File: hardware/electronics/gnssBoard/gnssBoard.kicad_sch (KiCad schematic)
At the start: 22 parts, among them J1 Standoff, J2 M.2_E_Key_PCB_Edge, U1 AP7361E

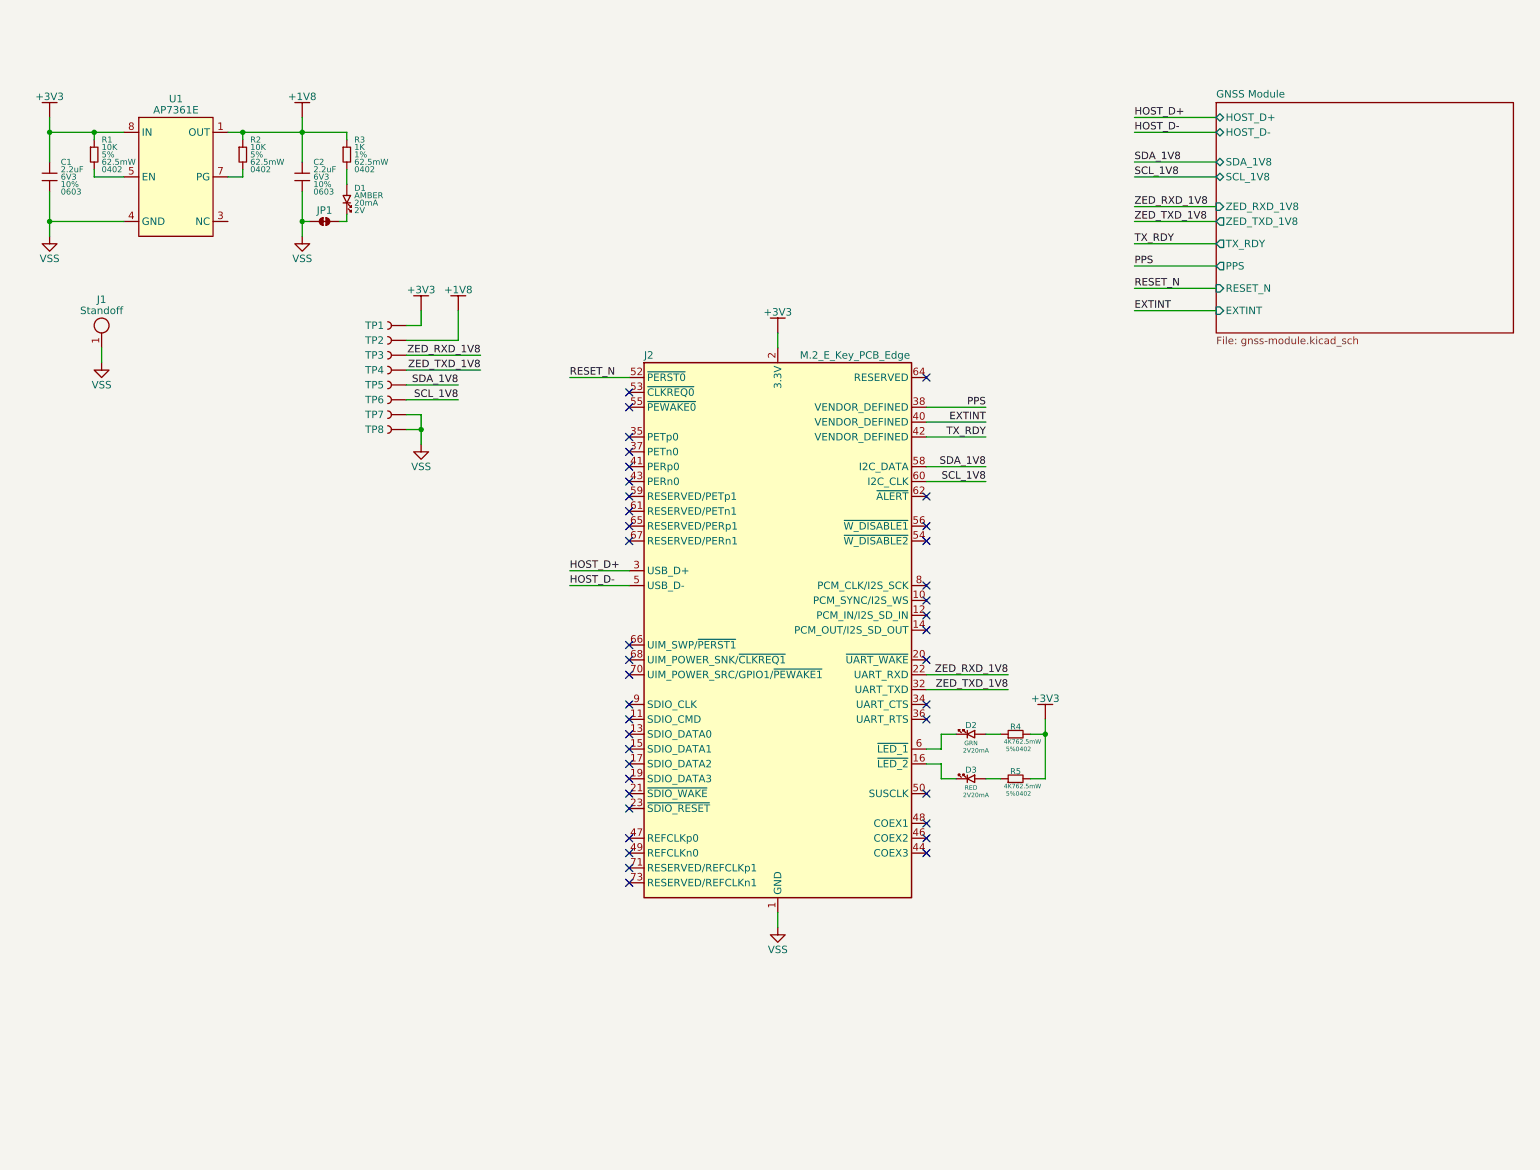
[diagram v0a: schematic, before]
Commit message: cleaned up schematic
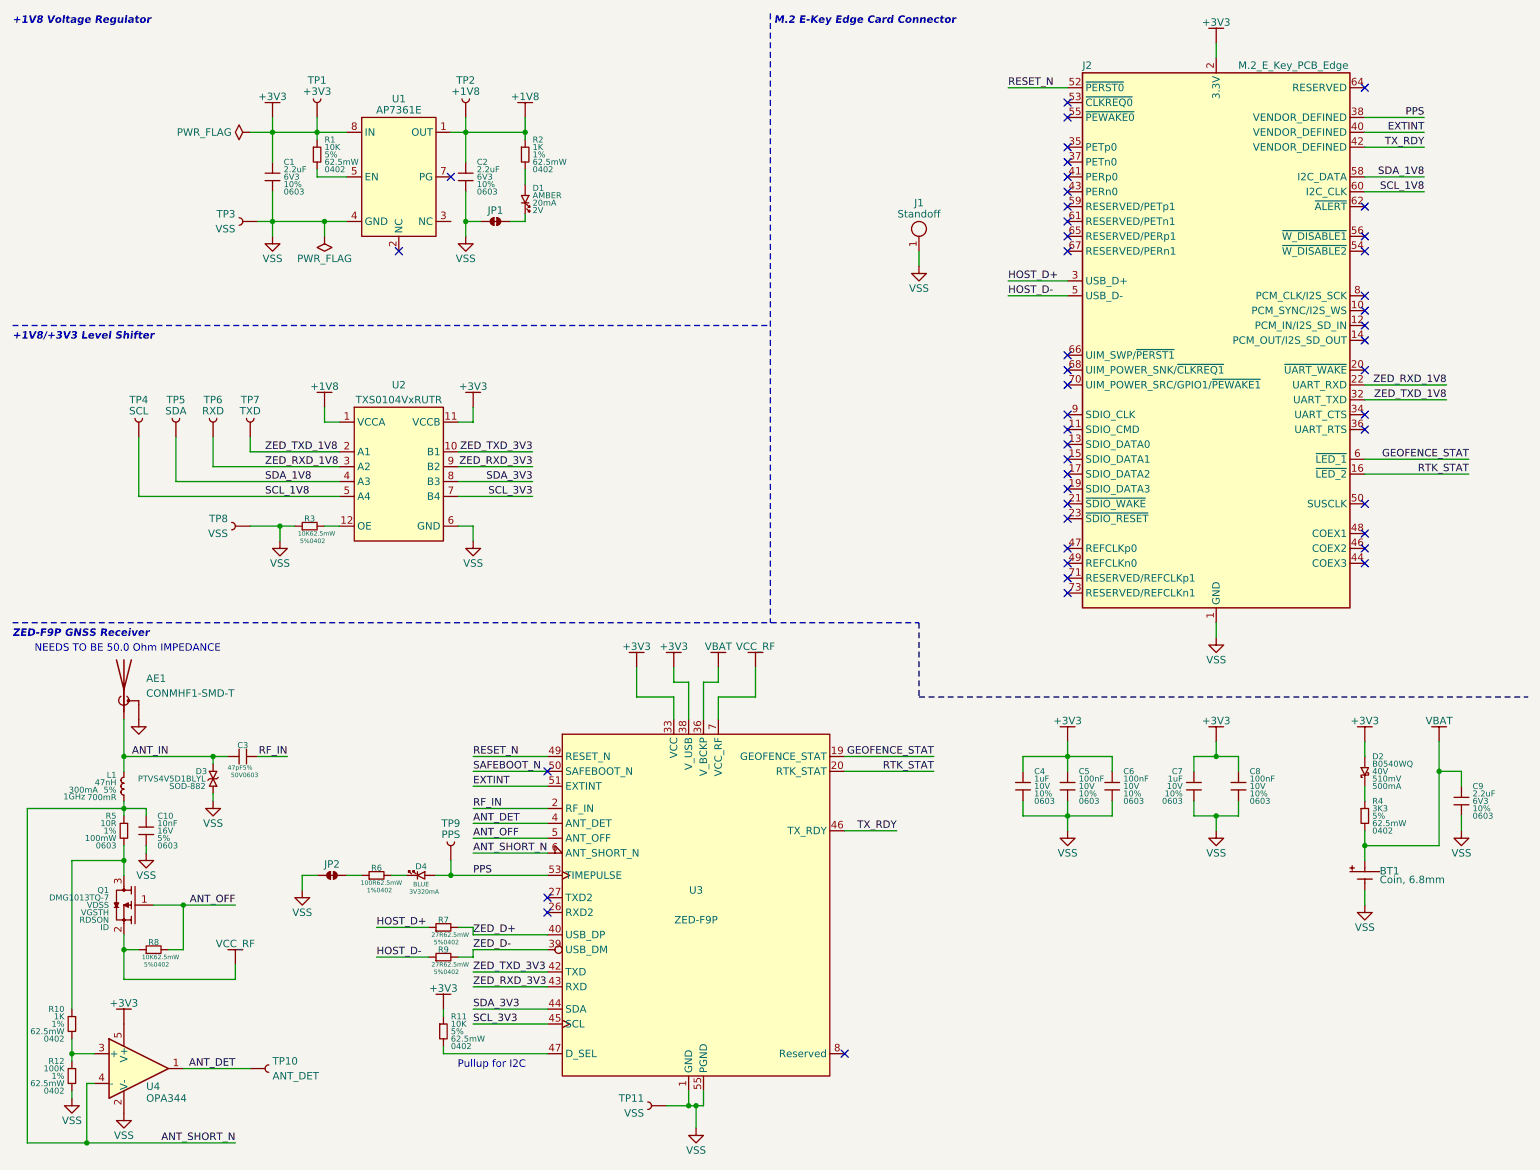
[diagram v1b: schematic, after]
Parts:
- removed D2: LTST-C190KGKT, lib_fp:LTST-0603, symbol lib_sch:LED_horizontal_1
- removed D3: LTST-C190KRKT, lib_fp:LTST-0603, symbol lib_sch:LED_horizontal_1
- removed R2: 10K, lib_fp:CRCW0402, symbol lib_sch:R
- removed R4, R5: 4K7, lib_fp:CRCW0402, symbol lib_sch:R_horizontal
- removed TP3, TP8: ~, lib_fp:TP_1mm, symbol lib_sch:Testpoint
- added AE1: CONMHF1-SMD-T, lib_fp:CONMHF1, symbol lib_sch:Antenna_Shield
- added BT1: ~, lib_fp:MS621FE-FL11E, symbol lib_sch:Battery
- added C10: 10nF, lib_fp:MLCC0603, symbol lib_sch:C
- added C3: 47pF, lib_fp:MLCC0603, symbol lib_sch:C_horizontal
- added C4, C7: 1uF, lib_fp:MLCC0603, symbol lib_sch:C
- added C5, C6, C8: 100nF, lib_fp:MLCC0603, symbol lib_sch:C
- added C9: 2.2uF, lib_fp:MLCC0603, symbol lib_sch:C
- added D2: B0540WQ, lib_fp:SOD123, symbol lib_sch:D_Schottky
- added D3: PTVS4V5D1BLYL, lib_fp:SOD882, symbol lib_sch:D_TVS
- added D4: LTST-C190KRKT, lib_fp:LTST-0603, symbol lib_sch:LED_horizontal_1
- added JP2: ~, lib_fp:SolderJumper-2_P1.3mm_Bridged_Pad1.0x1.5mm, symbol lib_sch:Jumper_2_Bridged
- added L1: 47nH, lib_fp:L_0402, symbol lib_sch:L
- added Q1: DMG1013TQ-7, lib_fp:SOT23-3P50_160X160X75L22X22N, symbol lib_sch:PMOS_DGS
- added R10: 1K, lib_fp:CRCW0402, symbol lib_sch:R
- added R11: 10K, lib_fp:CRCW0402, symbol lib_sch:R
- added R12: 100K, lib_fp:CRCW0402, symbol lib_sch:R
- added R3, R8: 10K, lib_fp:CRCW0402, symbol lib_sch:R_horizontal
- added R4: 3K3, lib_fp:CRCW0402, symbol lib_sch:R
- added R5: 10R, lib_fp:CRCW0603, symbol lib_sch:R
- added R6: 100R, lib_fp:CRCW0402, symbol lib_sch:R_horizontal
- added R7, R9: 27R, lib_fp:CRCW0402, symbol lib_sch:R_horizontal
- added TP10: ANT_DET, lib_fp:TP_1mm, symbol lib_sch:Testpoint_horizontal
- added TP11, TP3, TP8: VSS, lib_fp:TP_1mm, symbol lib_sch:Testpoint_horizontal
- added TP9: PPS, lib_fp:TP_1mm, symbol lib_sch:Testpoint
- added U2: TXS0104VxRUTR, lib_fp:RUT0012A, symbol lib_sch:TXS0104VxRUTR
- added U3: ZED-F9P, lib_fp:ZED-F9P-04B_UBL, symbol lib_sch:ZED-F9P-04B
- added U4: OPA344, lib_fp:SOT23-5P95_280X300X110L40X38N, symbol lib_sch:TS391
- J2: DKPN N/A -> (none); MPN N/A -> (none); Manufacturer N/A -> (none); now in the parts list
- JP1: footprint lib_fp:Jumper_2_Bridged -> lib_fp:SolderJumper-2_P1.3mm_Bridged_Pad1.0x1.5mm
- TP1: value ~ -> +3V3
- TP2: value ~ -> +1V8
- TP4: value ~ -> SCL
- TP5: value ~ -> SDA
- TP6: value ~ -> RXD
- TP7: value ~ -> TXD
- renumbered R3 to R2
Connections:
- net +1V8: now also U2.1 (VCCA)
- net +3V3: now also C4.1, C5.1, C6.1, C7.1, C8.1, D2.1, R11.1, U2.11 (VCCB), U3.33 (VCC), U3.34 (VCC), U3.38 (V_USB), U4.5 (V+)
- net EXTINT: now also U3.51 (EXTINT)
- net HOST_D+: now also R7.1
- net HOST_D-: now also R9.1
- net PPS: now also D4.1, TP9.1, U3.53 (TIMEPULSE)
- net RESET_N: now also U3.49 (RESET_N)
- net SCL_1V8: now also TP4.1, U2.5 (A4); no longer TP6.1
- net SDA_1V8: now also U2.4 (A3)
- net TX_RDY: now also U3.46 (TX_RDY)
- net VSS: now also AE1.2 (Shield), BT1.2, C10.2, C4.2, C5.2, C6.2, C7.2, C8.2, C9.2, D3.1, JP2.2, R12.2, R3.1, TP11.1, TP3.1, TP8.1, U2.6 (GND), U3.1 (GND), U3.100 (PGND), U3.101 (PGND), U3.102 (PGND), U3.12 (GND), U3.14 (GND), U3.3 (GND), U3.32 (GND), U3.37 (GND), U3.41 (GND), U3.48 (GND), U3.55 (PGND), U3.56 (PGND), U3.57 (PGND), U3.58 (PGND), U3.59 (PGND), U3.60 (PGND), U3.61 (PGND), U3.62 (PGND), U3.63 (PGND), U3.64 (PGND), U3.65 (PGND), U3.66 (PGND), U3.67 (PGND), U3.68 (PGND), U3.69 (PGND), U3.70 (PGND), U3.71 (PGND), U3.72 (PGND), U3.73 (PGND), U3.74 (PGND), U3.75 (PGND), U3.76 (PGND), U3.77 (PGND), U3.78 (PGND), U3.79 (PGND), U3.80 (PGND), U3.81 (PGND), U3.82 (PGND), U3.83 (PGND), U3.84 (PGND), U3.85 (PGND), U3.86 (PGND), U3.87 (PGND), U3.88 (PGND), U3.89 (PGND), U3.90 (PGND), U3.91 (PGND), U3.92 (PGND), U3.93 (PGND), U3.94 (PGND), U3.95 (PGND), U3.96 (PGND), U3.97 (PGND), U3.98 (PGND), U3.99 (PGND), U4.2 (V-); no longer TP7.1
- net ZED_RXD_1V8: now also TP6.1, U2.3 (A2)
- net ZED_TXD_1V8: now also TP7.1, U2.2 (A1); no longer TP4.1
- net RTK_STAT: now reaches J2.16 (~{LED_2})
- net RTK_STAT: now also U3.20 (RTK_STAT)
- net GEOFENCE_STAT: now reaches J2.6 (~{LED_1})
- net GEOFENCE_STAT: now also U3.19 (GEOFENCE_STAT)
- new net: Q1.3, R10.1, R5.2
- new net: R11.2, U3.47 (D_SEL)
- new net: R3.2, U2.12 (OE)
- new net: R10.2, R12.1, U4.3 (+)
- new net: U3.10 (Reserved), U3.11 (Reserved), U3.13 (Reserved), U3.15 (Reserved), U3.16 (Reserved), U3.17 (Reserved), U3.18 (Reserved), U3.21 (Reserved), U3.22 (Reserved), U3.23 (Reserved), U3.24 (Reserved), U3.25 (Reserved), U3.28 (Reserved), U3.29 (Reserved), U3.30 (Reserved), U3.31 (Reserved), U3.35 (Reserved), U3.52 (Reserved), U3.54 (Reserved), U3.8 (Reserved), U3.9 (Reserved)
- new net: JP2.1, R6.1
- new net: D4.2, R6.2
- new net: D2.2, R4.1
- new net ANT_DET: TP10.1, U3.4 (ANT_DET), U4.1
- new net ANT_IN: AE1.1 (A), C3.1, D3.2, L1.1
- new net ANT_OFF: Q1.1, R8.2, U3.5 (ANT_OFF)
- new net ANT_SHORT_N: C10.1, L1.2, R5.1, U3.6 (ANT_SHORT_N), U4.4 (-)
- new net RF_IN: C3.2, U3.2 (RF_IN)
- new net SAFEBOOT_N: U3.50 (SAFEBOOT_N)
- new net SCL_3V3: U2.7 (B4), U3.45 (SCL)
- new net SDA_3V3: U2.8 (B3), U3.44 (SDA)
- new net VBAT: BT1.1, C9.1, R4.2, U3.36 (V_BCKP)
- new net VCC_RF: Q1.2, R8.1, U3.7 (VCC_RF)
- new net ZED_D+: R7.2, U3.40 (USB_DP)
- new net ZED_D-: R9.2, U3.39 (USB_DM)
- new net ZED_RXD_3V3: U2.9 (B2), U3.43 (RXD)
- new net ZED_TXD_3V3: U2.10 (B1), U3.42 (TXD)
- no-connect marks 40 -> 46
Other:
- removed sheet GNSS Module
- note added: "+1V8 Voltage Regulator"
- note added: "+1V8/+3V3 Level Shifter"
- note added: "M.2 E-Key Edge Card Connector"
- note added: "NEEDS TO BE 50.0 Ohm IMPEDANCE"
- note added: "Pullup for I2C"
- note added: "ZED-F9P GNSS Receiver"
- moved on the sheet: C1, C2, D1, J1, J2, JP1, R1, R2

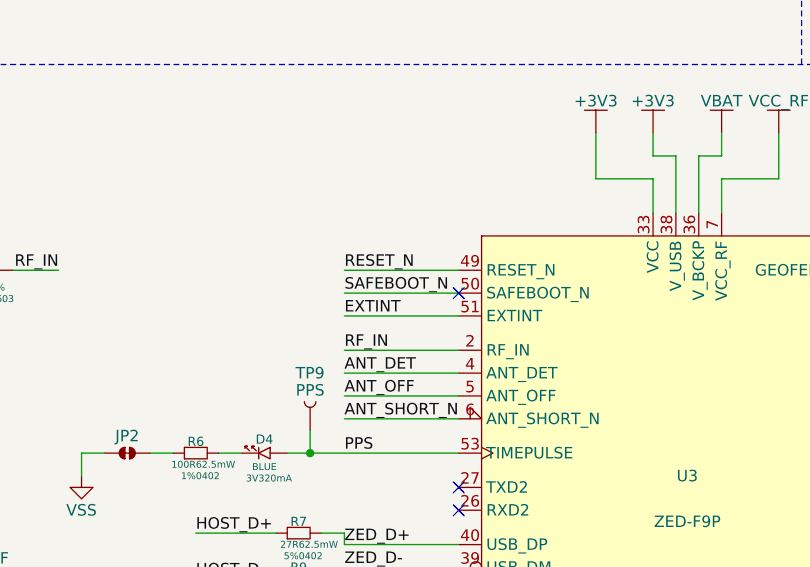
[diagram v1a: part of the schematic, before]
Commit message: changed TPs to exempt from BOM
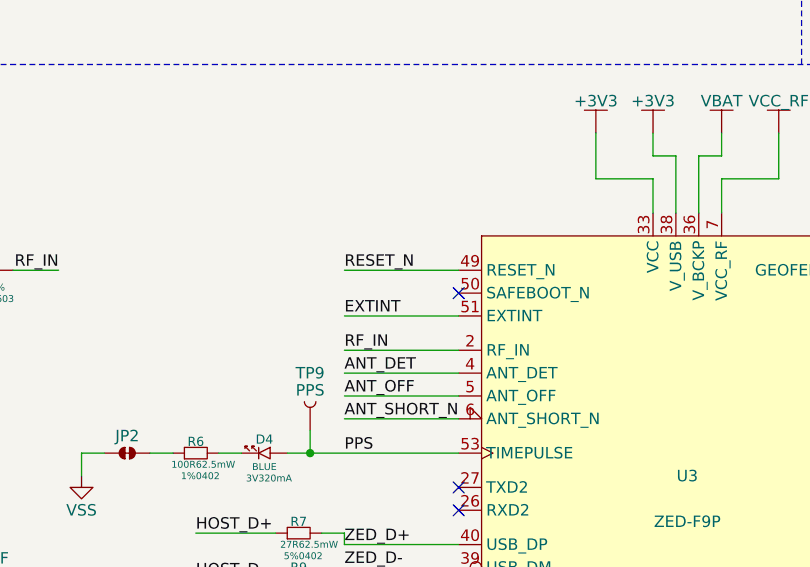
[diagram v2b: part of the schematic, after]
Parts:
- BT1: value ~ -> MS621FE-FL11E
- TP1, TP10, TP11, TP2, TP3, TP4, TP5, TP6, TP7, TP8, TP9: now left out of the parts list
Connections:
- net SAFEBOOT_N: no longer names the net of U3.50 (SAFEBOOT_N)
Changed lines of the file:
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@@
 	(title_block
 		(title "U-bolx ZED-F9P M.2 E-Key")
-		(date "2024-12-21")
+		(date "2024-12-23")
 		(rev "01")
 		(comment 2 "PROTOTYPE")
@@
 	(wire
 		(pts
-			(xy 88.9 139.7) (xy 101.6 139.7)
-		)
-		(stroke
-			(width 0)
-			(type default)
-		)
-	)
-	(wire
-		(pts
 			(xy 241.3 152.4) (xy 241.3 154.94)
 		)
@@
 		)
 	)
-	(label "SAFEBOOT_N"
-		(at 88.9 139.7 0)
-		(fields_autoplaced yes)
-		(effects
-			(font
-				(size 1.27 1.27)
-			)
-			(justify left bottom)
-		)
-	)
 	(label "ZED_TXD_3V3"
 		(at 99.06 85.09 180)
@@
 		(unit 1)
 		(exclude_from_sim no)
-		(in_bom yes)
+		(in_bom no)
 		(on_board yes)
 		(dnp no)
@@
 		(unit 1)
 		(exclude_from_sim no)
-		(in_bom yes)
+		(in_bom no)
 		(on_board yes)
 		(dnp no)
@@
 		(unit 1)
 		(exclude_from_sim no)
-		(in_bom yes)
+		(in_bom no)
 		(on_board yes)
 		(dnp no)
@@
 			)
 		)
-		(property "Value" "~"
+		(property "Value" "MS621FE-FL11E"
 			(at 241.3 157.48 0)
 			(do_not_autoplace yes)
@@
 		(unit 1)
 		(exclude_from_sim no)
-		(in_bom yes)
+		(in_bom no)
 		(on_board yes)
 		(dnp no)
@@
 		(unit 1)
 		(exclude_from_sim no)
-		(in_bom yes)
+		(in_bom no)
 		(on_board yes)
 		(dnp no)
@@
 		(unit 1)
 		(exclude_from_sim no)
-		(in_bom yes)
+		(in_bom no)
 		(on_board yes)
 		(dnp no)
@@
 		(unit 1)
 		(exclude_from_sim no)
-		(in_bom yes)
+		(in_bom no)
 		(on_board yes)
 		(dnp no)
@@
 		(unit 1)
 		(exclude_from_sim no)
-		(in_bom yes)
+		(in_bom no)
 		(on_board yes)
 		(dnp no)
@@
 		(unit 1)
 		(exclude_from_sim no)
-		(in_bom yes)
+		(in_bom no)
 		(on_board yes)
 		(dnp no)
@@
 		(unit 1)
 		(exclude_from_sim no)
-		(in_bom yes)
+		(in_bom no)
 		(on_board yes)
 		(dnp no)
@@
 		(unit 1)
 		(exclude_from_sim no)
-		(in_bom yes)
+		(in_bom no)
 		(on_board yes)
 		(dnp no)

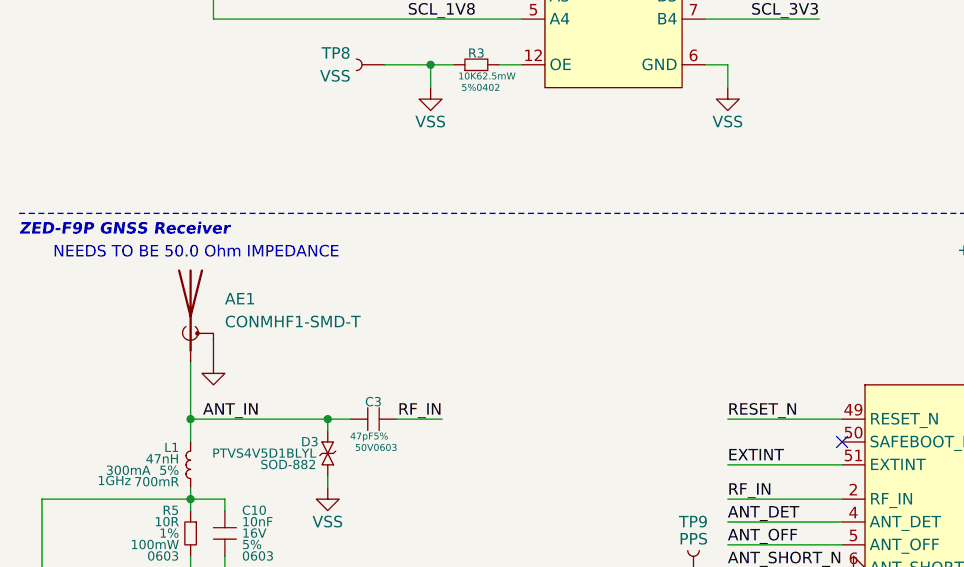
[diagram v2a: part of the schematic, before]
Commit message: added note for antenna feedline tracewidth
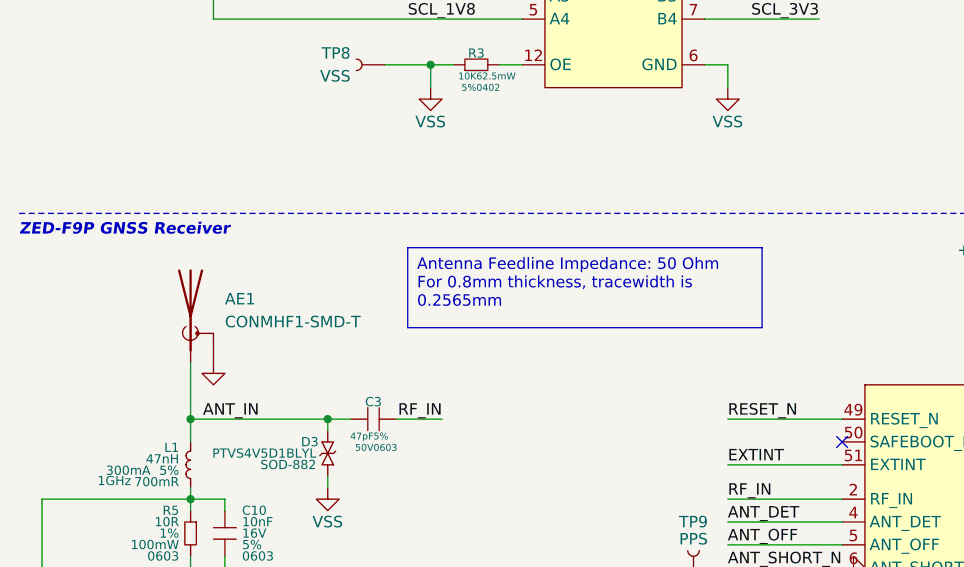
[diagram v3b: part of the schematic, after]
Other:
- note removed: "NEEDS TO BE 50.0 Ohm IMPEDANCE"
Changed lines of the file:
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@@
 	(title_block
 		(title "U-bolx ZED-F9P M.2 E-Key")
-		(date "2024-12-23")
+		(date "2025-01-01")
 		(rev "01")
 		(comment 2 "PROTOTYPE")
-		(comment 3 "2024")
+		(comment 3 "2025")
 	)
 	(junction
@@
 			(width 0)
 			(type default)
+		)
+	)
+	(text_box "Antenna Feedline Impedance: 50 Ohm\nFor 0.8mm thickness, tracewidth is 0.2565mm"
+		(exclude_from_sim no)
+		(at 53.34 118.11 0)
+		(size 39.37 8.89)
+		(stroke
+			(width 0)
+			(type default)
+		)
+		(fill
+			(type none)
+		)
+		(effects
+			(font
+				(size 1.27 1.27)
+			)
+			(justify left top)
 		)
 	)
@@
 		(effects
 			(font
-				(size 1.27 1.27)
-			)
-		)
-	)
-	(text "NEEDS TO BE 50.0 Ohm IMPEDANCE"
-		(exclude_from_sim no)
-		(at 29.845 118.745 0)
-		(effects
-			(font

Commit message: changes from design review
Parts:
- removed R2: 1K, lib_fp:CRCW0402, symbol lib_sch:R
- removed R3: 10K, lib_fp:CRCW0402, symbol lib_sch:R_horizontal
- removed TP8: VSS, lib_fp:TP_1mm, symbol lib_sch:Testpoint_horizontal
- added C11, C12: 100nF, lib_fp:MLCC0603, symbol lib_sch:C
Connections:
- net +1V8: now also D1.1, U2.12 (OE), C11.1
- net +3V3: now also C12.1
- net VSS: now also C11.2, C12.2
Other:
- note added: "Place close to pin 38"
- note added: "Place close to pins 33/34"
- moved on the sheet: D1
